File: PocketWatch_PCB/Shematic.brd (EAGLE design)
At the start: 53 x 56 mm, 44 parts, among them U2 ATTINY88-AU

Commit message: Added Dimensions
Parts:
- removed T1, T2, T3, T4: (no value), transistor:SOT23-BEC
- added IC1: 74HC139D, 74xx-eu:SO16
- added Q1, Q2, Q3, Q4: BCX71SMD, transistor-pnp:SOT23
- added Q5, Q6, Q7, Q8: (no value), transistor-npn:SOT23
- added SV4: (no value), con-lstb:MA05-1
- moved R5 36.7 mm to (57.0, 15.0)
- moved R6 36.7 mm to (62.5, 15.0)
- moved R8 34.0 mm to (65.5, 15.0)
- moved R7 31.4 mm to (59.5, 15.0)
- moved GND 12.5 mm to (5.50, 53.0)
- moved VCC 12.5 mm to (2.50, 53.0)
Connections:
- net TG0_2 renamed T0_2
- net TG1_2 renamed T1_2
- net TG2_2 renamed T2_2
- net TG3_2 renamed T3_2
- removed net EN0: R5.1, U2.19
- removed net EN1: R6.1, U2.22
- removed net EN2: R7.1, U2.3
- removed net EN3: R8.1, U2.6
- removed net TG0: SV5.4, T1.C
- removed net TG1: SV5.3, T2.C
- removed net TG2: SV5.2, T3.C
- removed net TG3: SV5.1, T4.C
- new net HEF: U2.20
- new net M0: Q5.1, U2.19
- new net M1: Q6.1, U2.22
- new net M2: Q7.1, U2.3
- new net M3: Q8.1, U2.6
- new net N$10: IC1.5, R6.1
- new net N$11: IC1.6, R7.1
- new net N$13: IC1.7, R8.1
- new net N$18: IC1.9, R14.2
- new net N$19: Q5.3, SV4.1
- new net N$20: Q6.3, SV4.2
- new net N$21: Q7.3, SV4.3
- new net N$22: Q8.3, SV4.4
- new net N$27: IC1.13, U2.7
- new net N$28: IC1.14, U2.8
- new net N$8: IC1.4, R5.1
- new net T0: Q1.3, SV5.4
- new net T1: Q2.3, SV5.3
- new net T2: Q3.3, SV5.2
- new net T3: Q4.3, SV5.1
- new net TC0: IC1.2, U2.12
- new net TC1: IC1.3, U2.13
- net GND: now also IC1.1, IC1.15, IC1.8, Q5.2, Q6.2, Q7.2, Q8.2; no longer AM.K, COLIN1.K, COLIN2.K, PM.K, T1.E, T2.E, T3.E, T4.E
- net N$1: now also Q4.1; no longer T4.B
- net N$15: now also IC1.12, R17.2; no longer R14.2, R15.2, U2.12
- net N$16: now also IC1.11, R16.2; no longer R17.2, U2.14
- net N$17: now also IC1.10, R15.2; no longer R16.2, U2.13
- net N$2: now also Q3.1; no longer T3.B
- net N$3: now also Q2.1; no longer T2.B
- net N$5: now also Q1.1; no longer T1.B
- net VCC: now also AM.K, COLIN1.K, COLIN2.K, IC1.16, PM.K, Q1.2, Q2.2, Q3.2, Q4.2, SV4.5
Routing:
- net EN3: track 26.0 -> 0.00 mm, vias 1 -> 0
- net EN2: track 20.5 -> 0.00 mm, vias 1 -> 0
- net EN1: track 16.7 -> 0.00 mm, vias 1 -> 0
- net EN0: track 13.4 -> 0.00 mm, vias 1 -> 0
- net SEG_G: track 11.9 -> 0.00 mm
- net SCL: track 44.9 -> 34.0 mm, vias 2 -> 1
- net SEG_DOT: track 10.5 -> 0.00 mm
- net MOSI: track 10.4 -> 0.00 mm
- net SCK: track 10.1 -> 0.00 mm
- net SEG_F: track 10.1 -> 0.00 mm
- net SEG_A: track 9.18 -> 0.00 mm
- net MISO: track 9.08 -> 0.00 mm
- net SDA: track 41.4 -> 32.8 mm, vias 2 -> 1
- net SEG_B: track 8.21 -> 0.00 mm
- net SEG_D: track 8.10 -> 0.00 mm
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
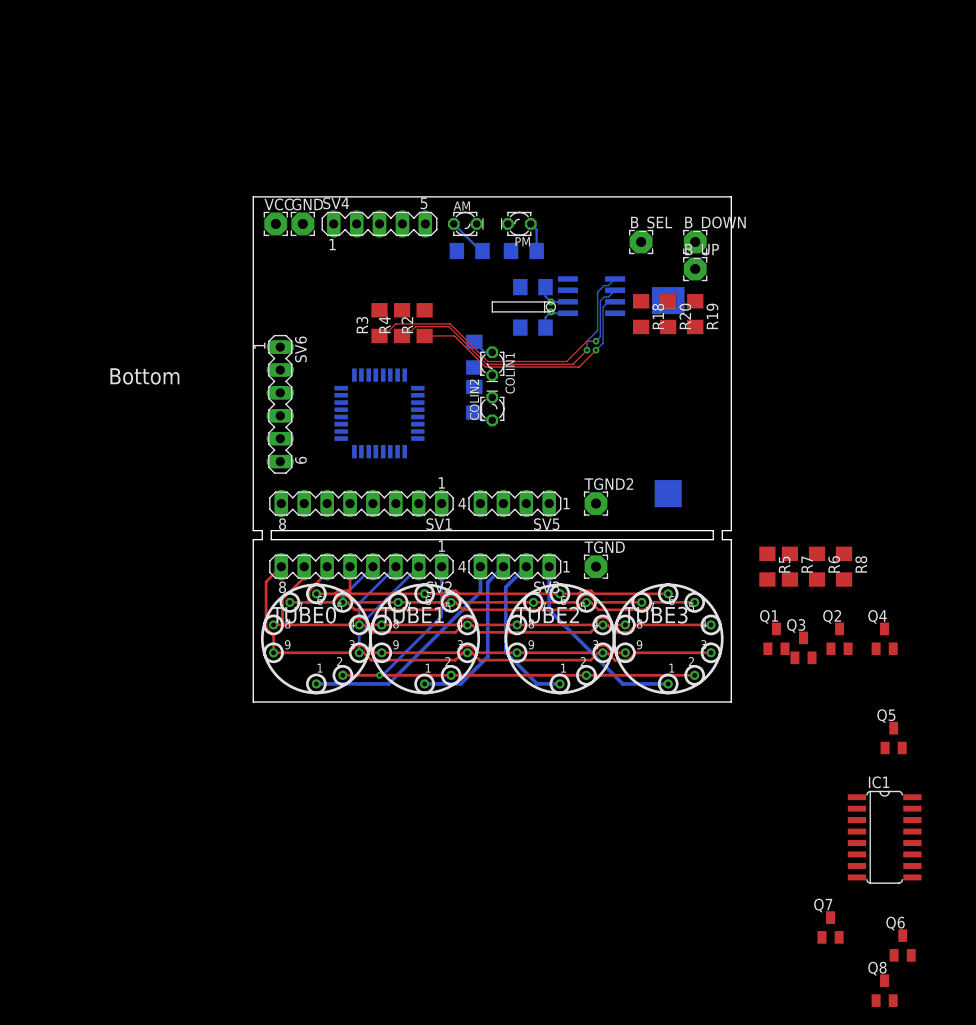
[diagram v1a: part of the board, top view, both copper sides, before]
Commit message: Completed most of the routing
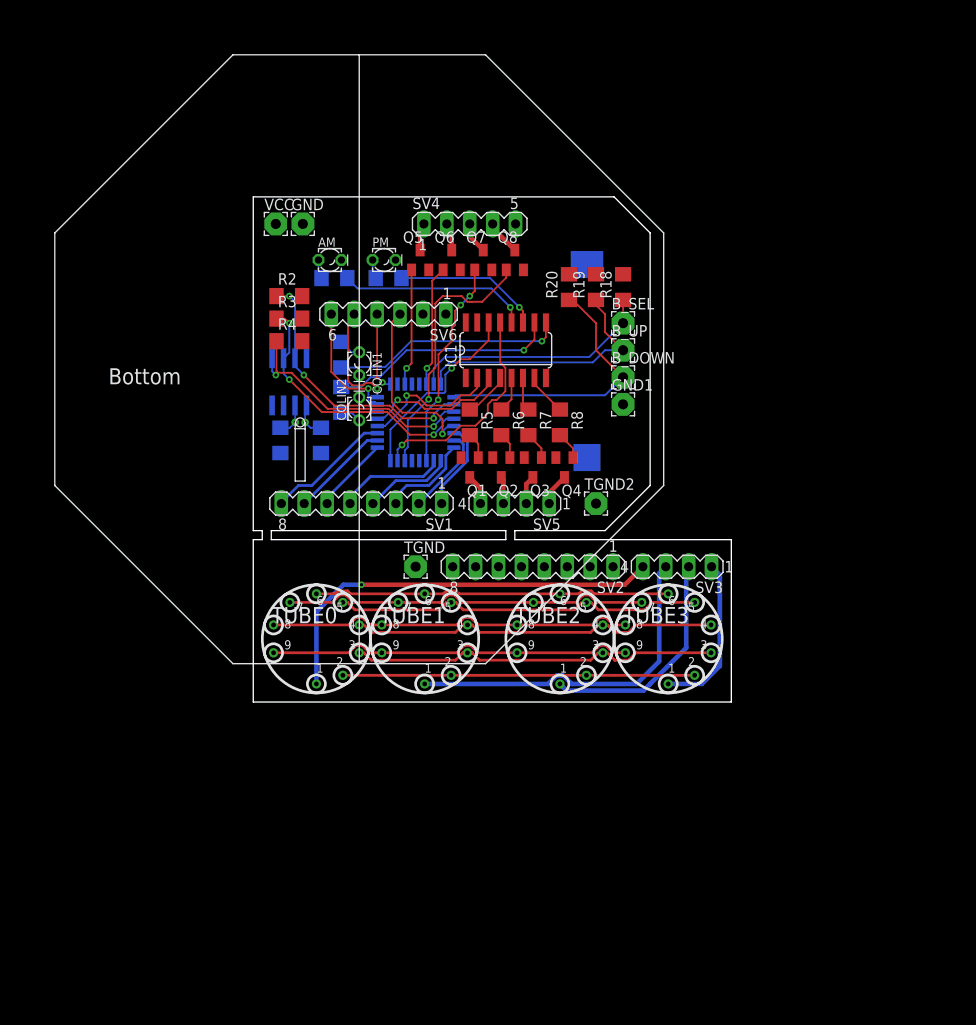
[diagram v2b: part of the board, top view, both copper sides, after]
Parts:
- added GND1: WIREPAD2,54/1,1, wirepad:2,54/1,1
- moved Q6 91.0 mm to (22.0, 49.0)
- moved Q8 90.8 mm to (29.0, 49.0)
- moved Q7 83.4 mm to (25.5, 49.0)
- moved Q5 74.6 mm to (18.5, 49.0)
- moved IC1 68.4 mm to (28.0, 39.0), turned to 0 degrees
- moved Q2 42.0 mm to (27.5, 26.0), turned to 180 degrees
- moved Q4 40.3 mm to (34.5, 26.0), turned to 180 degrees
- moved Q1 38.9 mm to (24.0, 26.0), turned to 180 degrees
- moved R6 38.5 mm to (27.5, 31.0)
- moved R5 36.7 mm to (24.0, 31.0)
- moved Q3 36.1 mm to (31.0, 26.0), turned to 180 degrees
- moved R8 35.3 mm to (34.0, 31.0)
- moved MCP7940M 34.8 mm to (4.00, 35.5), turned to 0 degrees
- moved R7 33.1 mm to (30.5, 31.0)
- moved C1 32.8 mm to (3.00, 29.0), turned to 270 degrees
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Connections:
- net GND: now also GND1.1
- net N$12: now also PM.A; no longer AM.A
- net N$14: now also AM.A; no longer PM.A
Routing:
- net B_DOWN: track 0.00 -> 31.0 mm
- net B_UP: track 0.00 -> 29.4 mm
- net M3: track 0.00 -> 29.3 mm, vias 0 -> 1
- net B_SEL: track 0.00 -> 27.4 mm
- net N$18: track 0.00 -> 26.0 mm, vias 0 -> 1
- net N$17: track 0.00 -> 25.5 mm, vias 0 -> 1
- net N$27: track 0.00 -> 24.3 mm, vias 0 -> 1
- net M2: track 0.00 -> 23.4 mm, vias 0 -> 3
- net N$28: track 0.00 -> 21.5 mm, vias 0 -> 1
- net N$15: track 0.00 -> 21.2 mm, vias 0 -> 1
- net T0_2: track 25.2 -> 46.3 mm, vias 0 -> 1
- net RESET: track 0.00 -> 20.0 mm, vias 0 -> 1
- net T1_2: track 19.0 -> 38.6 mm
- net TC0: track 0.00 -> 16.4 mm, vias 0 -> 1
- net N$16: track 0.00 -> 16.3 mm, vias 0 -> 1
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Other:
- outline, holes or cut-outs redrawn

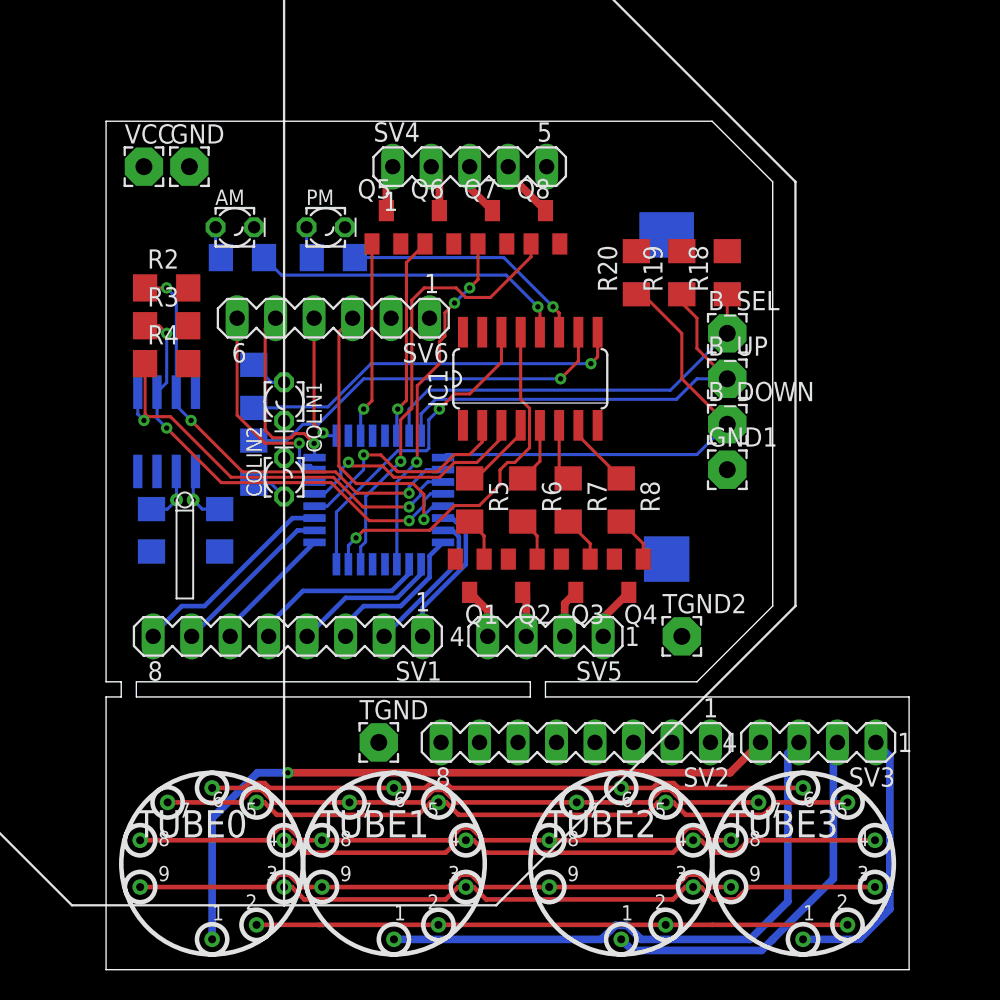
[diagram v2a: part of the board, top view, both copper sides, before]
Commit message: Completed PCB layout. Passes DRC.
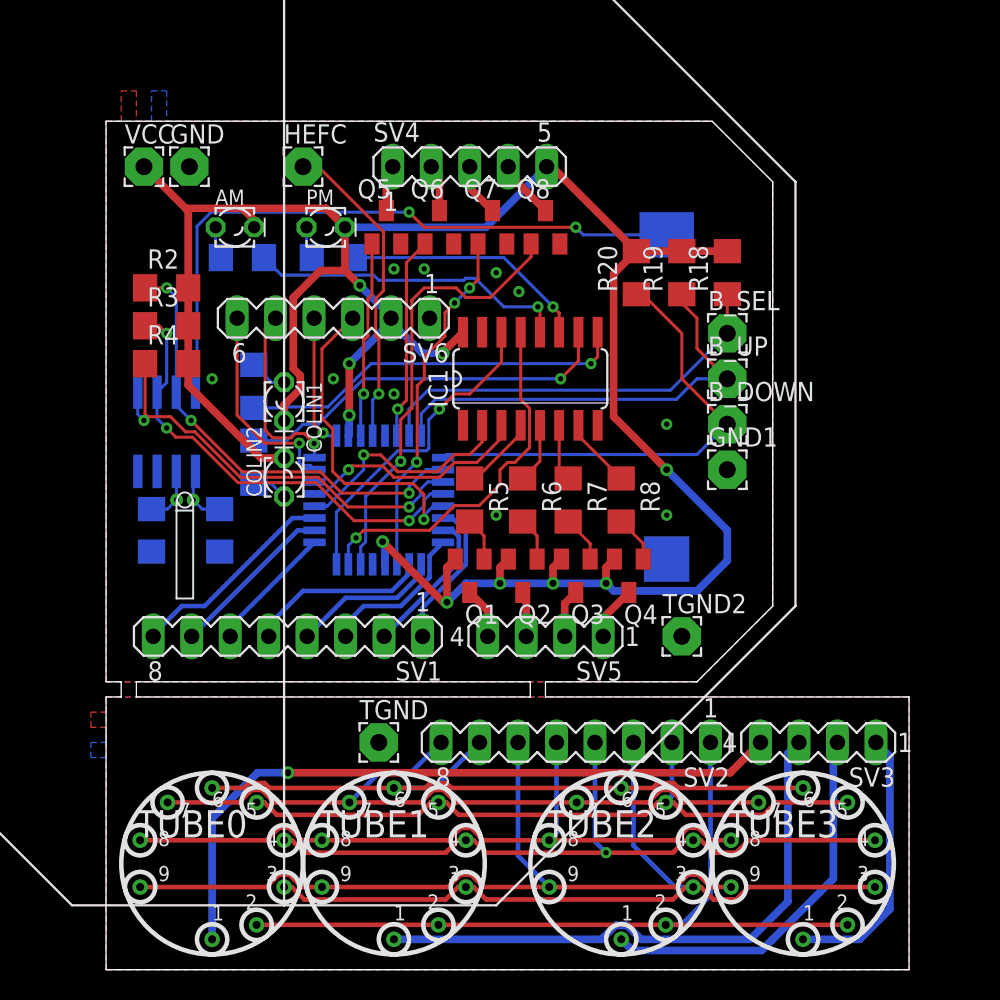
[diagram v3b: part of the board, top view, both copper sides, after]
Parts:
- added HEFC: (no value), wirepad:2,54/1,1
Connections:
- net HEF: now also HEFC.1
- net SEG_A_2: now also SV2.2; no longer SV2.4
- net SEG_B_2: now also SV2.3; no longer SV2.2
- net SEG_C_2: now also SV2.4; no longer SV2.3
- net SEG_D_2: now also SV2.5; no longer SV2.7
- net SEG_E_2: now also SV2.6; no longer SV2.8
- net SEG_F_2: now also SV2.7; no longer SV2.5
- net SEG_G_2: now also SV2.8; no longer SV2.6
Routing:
- net VCC: track 0.00 -> 161.4 mm, vias 0 -> 10
- net COIN: track 0.00 -> 43.0 mm, vias 0 -> 2
- net HEF: track 0.00 -> 21.0 mm, vias 0 -> 1
- net SEG_DOT_2: track 39.6 -> 52.9 mm
- net SEG_B_2: track 41.0 -> 52.9 mm
- net SEG_E_2: track 41.0 -> 51.4 mm
- net SEG_G_2: track 41.1 -> 48.7 mm
- net SEG_C_2: track 41.0 -> 48.6 mm, vias 0 -> 1
- net SEG_F_2: track 39.8 -> 46.7 mm
- net SEG_D_2: track 41.0 -> 47.7 mm
- net SEG_A_2: track 41.0 -> 45.2 mm
- net RESET: track 20.0 -> 21.3 mm
- added copper zone on layer 1, net GND
- added copper zone on layer 16, net GND
- added copper zone on layer 1, net TGND
- added copper zone on layer 16, net TGND

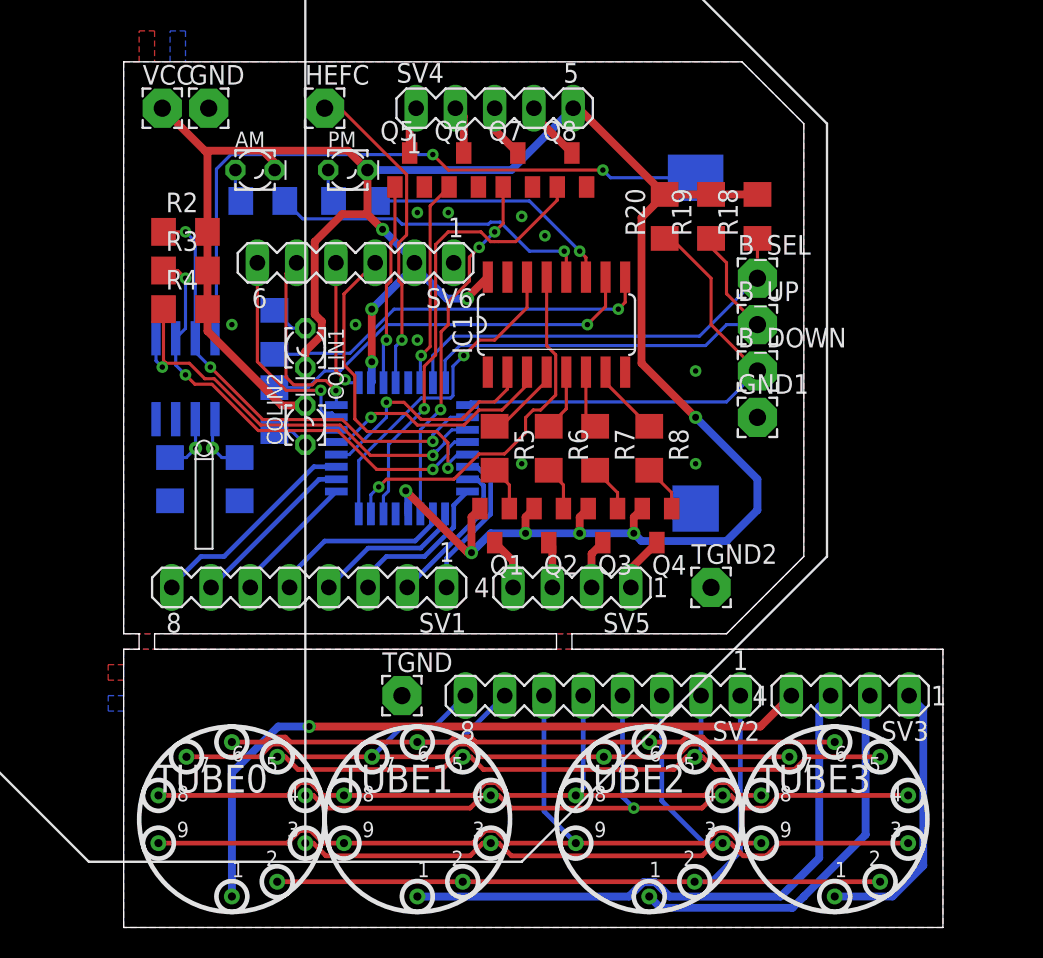
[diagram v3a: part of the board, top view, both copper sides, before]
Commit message: Added drill holes
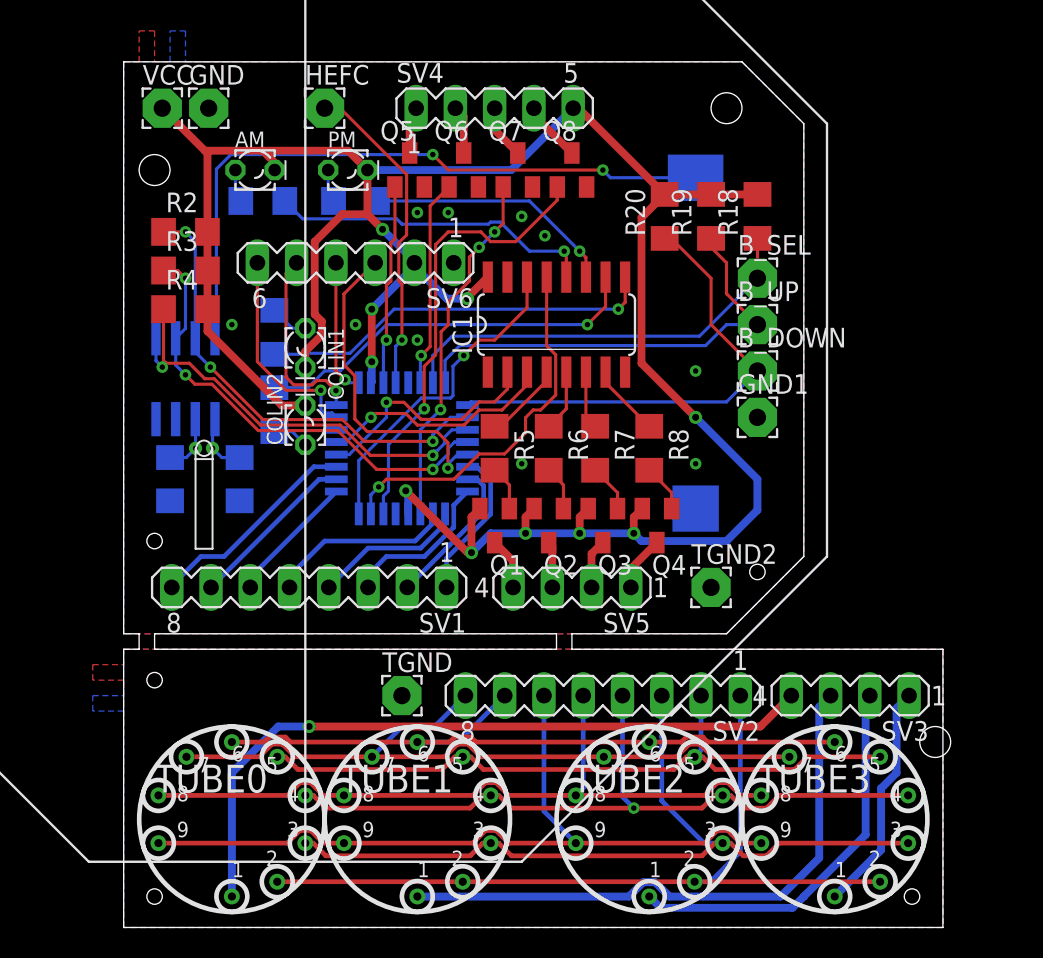
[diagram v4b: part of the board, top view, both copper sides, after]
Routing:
- net T3_2: track 17.9 -> 15.0 mm
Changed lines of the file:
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@@
 <dimension x1="151.75" y1="94" x2="165.75" y2="94" x3="158.75" y3="94" textsize="1.778" layer="21" width="0.01"/>
 <wire x1="11.75" y1="71.75" x2="11.75" y2="4.25" width="0.1524" layer="21"/>
+<hole x="2" y="25" drill="1"/>
+<hole x="2" y="49" drill="2"/>
+<hole x="39" y="53" drill="2"/>
+<hole x="41" y="23" drill="1"/>
+<hole x="2" y="16" drill="1"/>
+<hole x="2" y="2" drill="1"/>
+<hole x="51" y="2" drill="1"/>
+<hole x="52.5" y="12" drill="2"/>
 </plain>
 <attributes>
@@
 <contactref element="TUBE3" pad="1"/>
 <contactref element="SV3" pad="1"/>
-<wire x1="50.81" y1="15" x2="51.73" y2="14.08" width="0.508" layer="16"/>
-<wire x1="51.73" y1="14.08" x2="51.73" y2="4" width="0.508" layer="16"/>
-<wire x1="51.73" y1="4" x2="49.7356" y2="2.0056" width="0.508" layer="16"/>
-<wire x1="49.7356" y1="2.0056" x2="46" y2="2.0056" width="0.508" layer="16"/>
+<wire x1="46" y1="2.0056" x2="49" y2="5.0056" width="0.508" layer="16"/>
+<wire x1="49" y1="9" x2="49" y2="5.0056" width="0.508" layer="16"/>
+<wire x1="50.81" y1="15" x2="50" y2="14.19" width="0.508" layer="16"/>
+<wire x1="50" y1="10" x2="49" y2="9" width="0.508" layer="16"/>
+<wire x1="50" y1="14.19" x2="50" y2="10" width="0.508" layer="16"/>
 </signal>
 <signal name="T0">
@@
 <vertex x="0" y="0"/>
 <vertex x="0" y="16"/>
-<vertex x="-1" y="16"/>
-<vertex x="-1" y="17"/>
+<vertex x="-2" y="16"/>
+<vertex x="-2" y="17"/>
 <vertex x="0" y="17"/>
 </polygon>
@@
 <vertex x="0" y="0"/>
 <vertex x="0" y="14"/>
-<vertex x="-1" y="14"/>
-<vertex x="-1" y="15"/>
+<vertex x="-2" y="14"/>
+<vertex x="-2" y="15"/>
 <vertex x="0" y="15"/>
 </polygon>
